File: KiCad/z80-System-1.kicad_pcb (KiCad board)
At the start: 2 copper layers, 22 parts, among them J1 FTDI Header, SW1 Reset button, SW2 NMI Button, U1 62256, U2 Z80CPU, U3 AT28C64, U4 16550, U5 74LS04, U6 74LS32, X1 ACO-1.8432MHz

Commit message: Layout 1 finished
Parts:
- added REF**: MountingHole_2.2mm_M2, MountingHole:MountingHole_2.2mm_M2, F.Cu at (157.0, 144.0)
- added REF**: MountingHole_2.2mm_M2, MountingHole:MountingHole_2.2mm_M2, F.Cu at (237.0, 144.0)
- added REF**: MountingHole_2.2mm_M2, MountingHole:MountingHole_2.2mm_M2, F.Cu at (157.0, 54.0)
- added REF**: MountingHole_2.2mm_M2, MountingHole:MountingHole_2.2mm_M2, F.Cu at (237.0, 54.0)
- moved X1 17.0 mm to (181.6, 116.8), turned to 180 degrees
- moved C4 5.08 mm to (205.7, 55.9), turned to 180 degrees
- moved C5 5.08 mm to (231.1, 55.9), turned to 180 degrees
- moved C6 5.00 mm to (180.3, 55.9), turned to 180 degrees
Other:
- board outline added: 86 x 96 mm

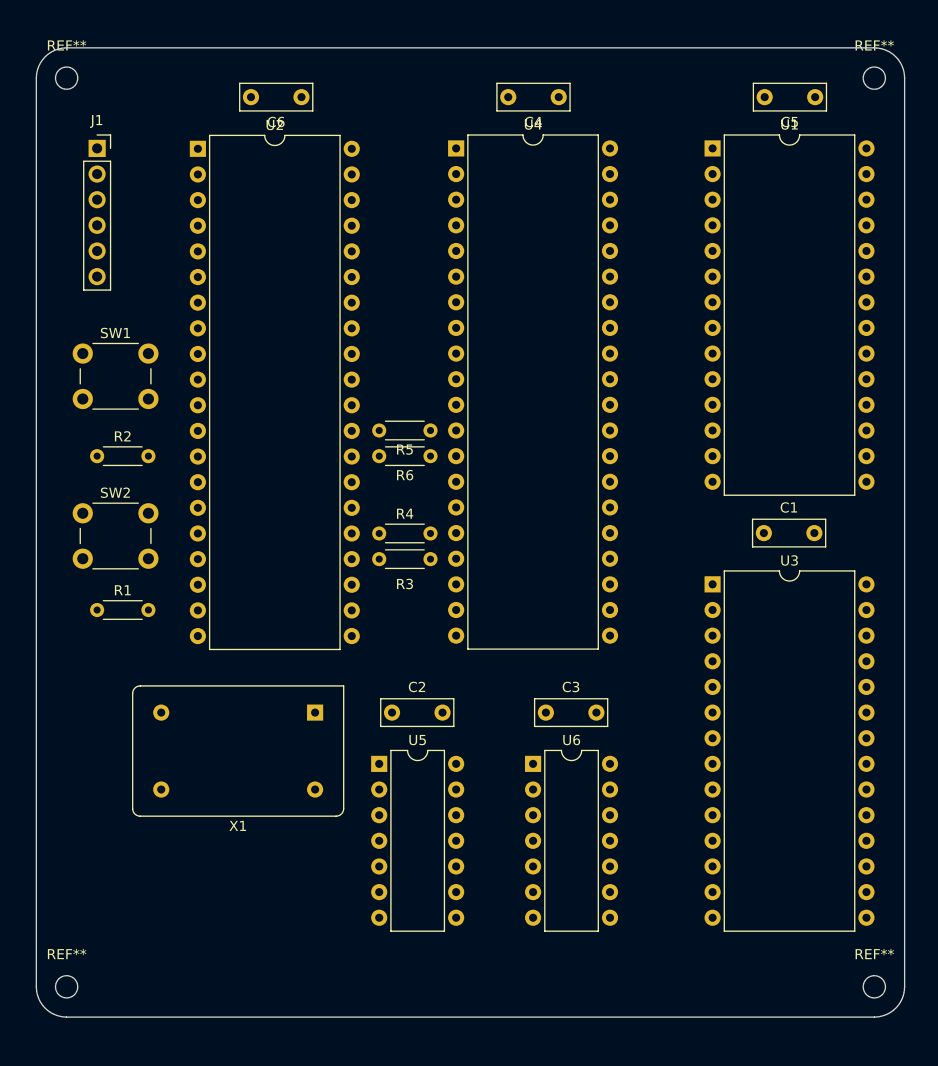
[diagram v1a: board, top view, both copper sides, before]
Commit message: Completed power rail and silk layer
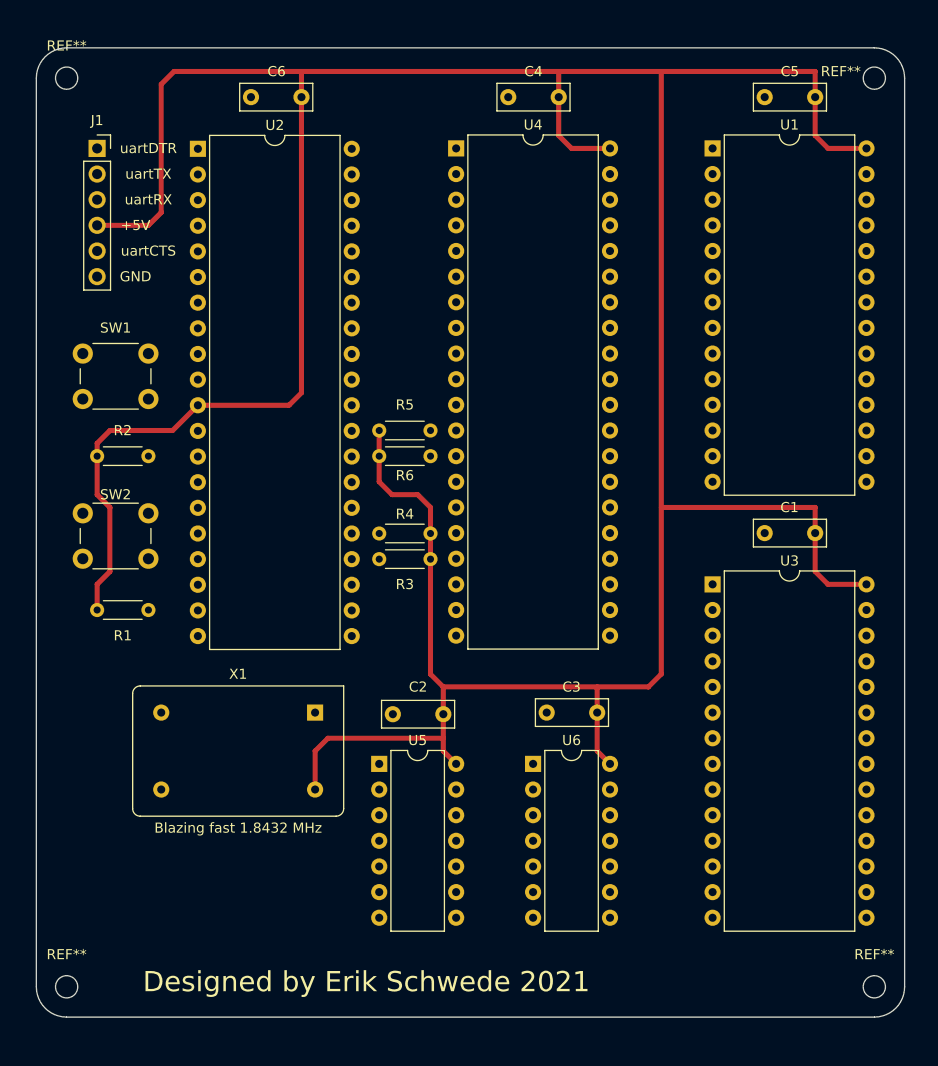
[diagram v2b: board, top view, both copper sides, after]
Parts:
- moved C2 5.08 mm to (194.3, 117.0), turned to 180 degrees
- moved C3 5.08 mm to (209.6, 116.8), turned to 180 degrees
- moved C1 5.08 mm to (231.1, 99.1), turned to 180 degrees
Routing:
- net +5V: track 0.00 -> 352.4 mm
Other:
- board text added: "+5V"
- board text added: "Blazing fast 1.8432 MHz"
- board text added: "Designed by Erik Schwede 2021"
- board text added: "GND"
- board text added: "uartCTS"
- board text added: "uartDTR"
- board text added: "uartRX"
- board text added: "uartTX"

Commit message: text
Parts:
- renumbered REF** to 1, REF** to 2, REF** to 3, REF** to 4
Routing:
- net ~CE_ROM: track 0.00 -> 54.4 mm
- net /D7: track 0.00 -> 50.6 mm
- net /D6: track 0.00 -> 50.6 mm
- net /A10: track 0.00 -> 50.1 mm
- net /D4: track 0.00 -> 50.1 mm, vias 0 -> 1
- net /A8: track 0.00 -> 48.8 mm, vias 0 -> 1
- net /D5: track 0.00 -> 48.0 mm
- net /A9: track 0.00 -> 48.0 mm, vias 0 -> 1
- net /D3: track 0.00 -> 46.6 mm
- net /A11: track 0.00 -> 46.2 mm
- net Net-(R2-Pad2): track 0.00 -> 40.5 mm
- net Net-(R1-Pad2): track 0.00 -> 16.5 mm

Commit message: Autoroute
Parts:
- renumbered 1 to M1, 2 to M2, 4 to M3, 3 to M4
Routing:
- net GND: track 0.00 -> 315.5 mm, vias 0 -> 1
- net /D3: track 46.6 -> 217.9 mm
- net /D7: track 50.6 -> 197.6 mm, vias 0 -> 1
- net /D0: track 0.00 -> 146.9 mm, vias 0 -> 2
- net /D4: track 50.1 -> 186.1 mm, vias 1 -> 2
- net /D1: track 0.00 -> 130.0 mm, vias 0 -> 2
- net /D2: track 0.00 -> 128.2 mm, vias 0 -> 3
- net A15: track 0.00 -> 112.1 mm
- net /A6: track 0.00 -> 107.4 mm, vias 0 -> 2
- net /A12: track 0.00 -> 105.7 mm, vias 0 -> 1
- net ~RD: track 0.00 -> 102.2 mm, vias 0 -> 2
- net /A2: track 0.00 -> 100.1 mm
- net ~WR: track 0.00 -> 96.6 mm, vias 0 -> 1
- net /D6: track 50.6 -> 146.0 mm, vias 0 -> 2
- net /A5: track 0.00 -> 87.1 mm, vias 0 -> 1
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
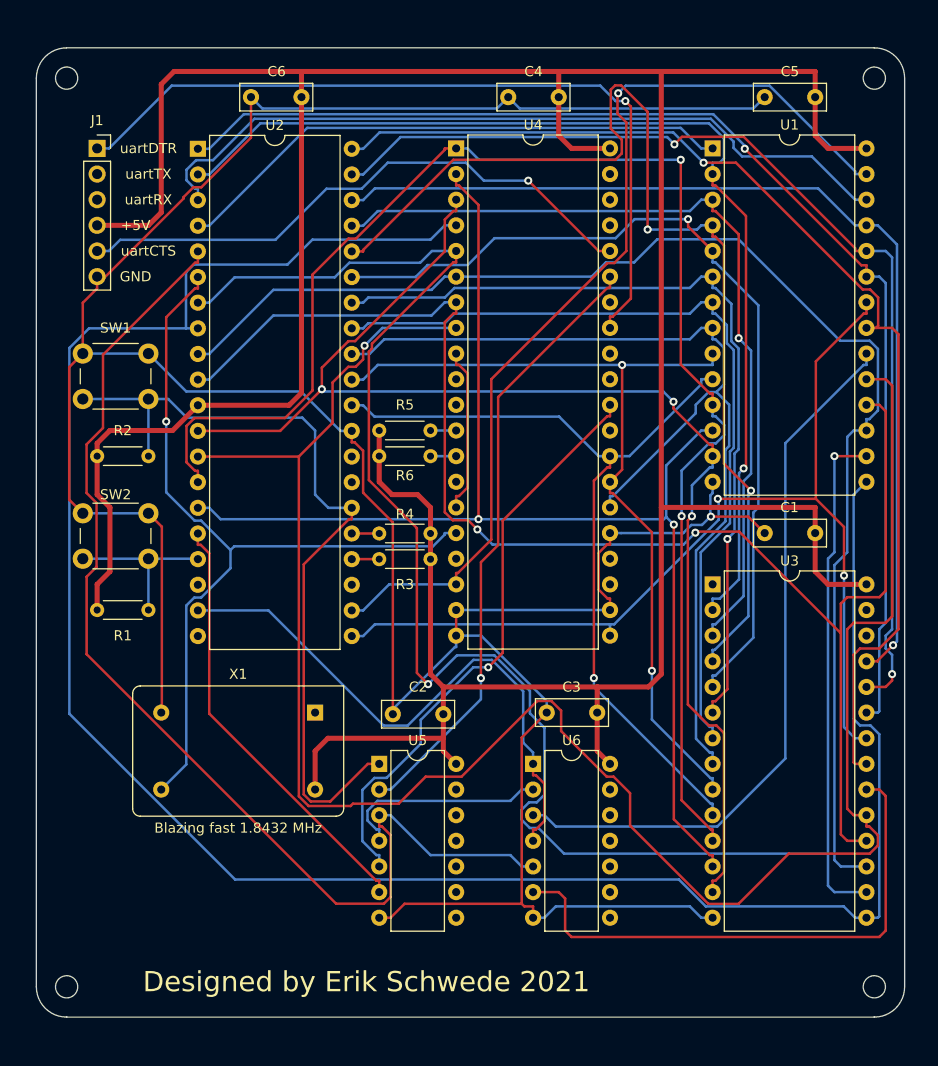
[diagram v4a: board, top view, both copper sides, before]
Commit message: Finished Routing
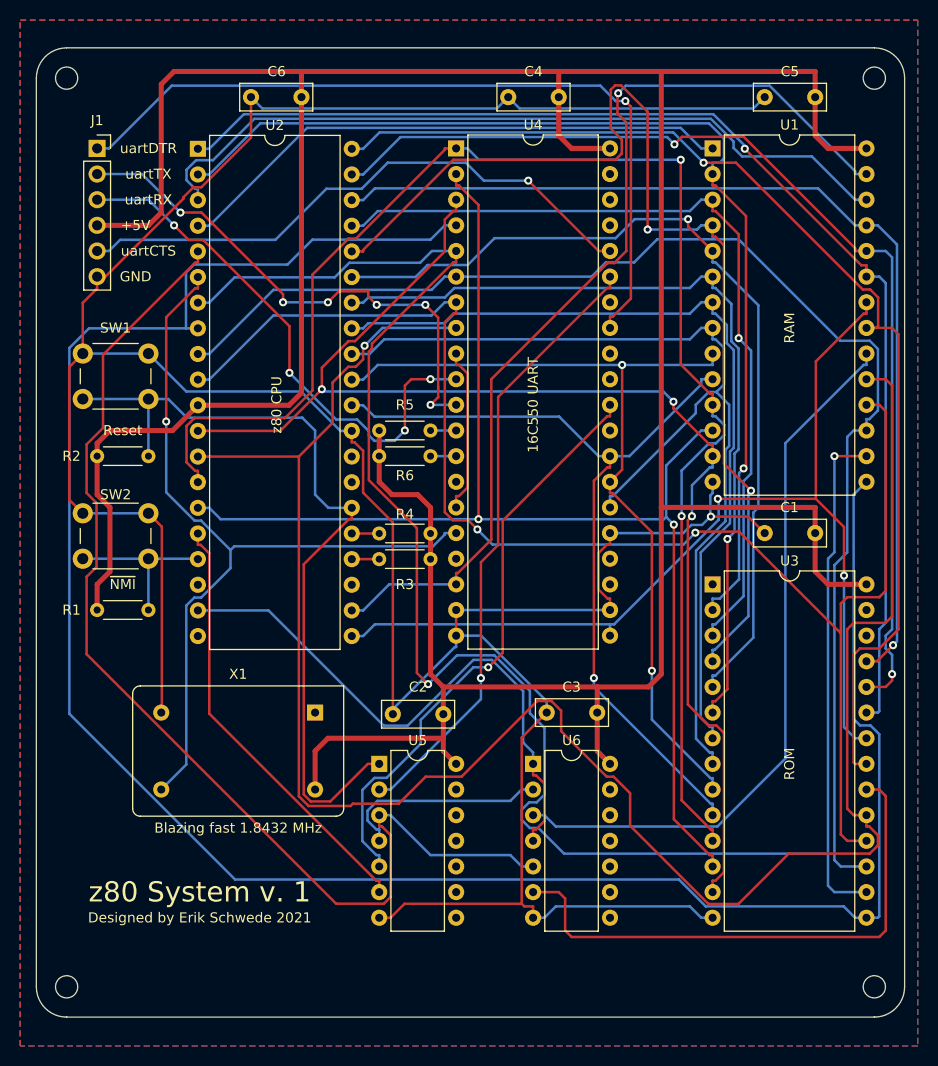
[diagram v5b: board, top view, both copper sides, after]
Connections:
- U4 pad 10: RX -> uartRX
- U4 pad 11: TX -> uartTX
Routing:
- net uartRX: track 0.00 -> 53.5 mm, vias 0 -> 4
- net uartTX: track 0.00 -> 52.8 mm, vias 0 -> 6
- added copper zone on B.Cu, net GND
- added copper zone on F.Cu, net GND
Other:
- board text added: "16C550 UART"
- board text added: "RAM"
- board text added: "ROM"
- board text added: "Reset"
- board text added: "z80 CPU"
- board text added: "z80 System v. 1"
- board text added: "~NMI"
